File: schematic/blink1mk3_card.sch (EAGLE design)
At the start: 15 parts, among them U1 EFM32HG309F64G, X2 USBPCB2

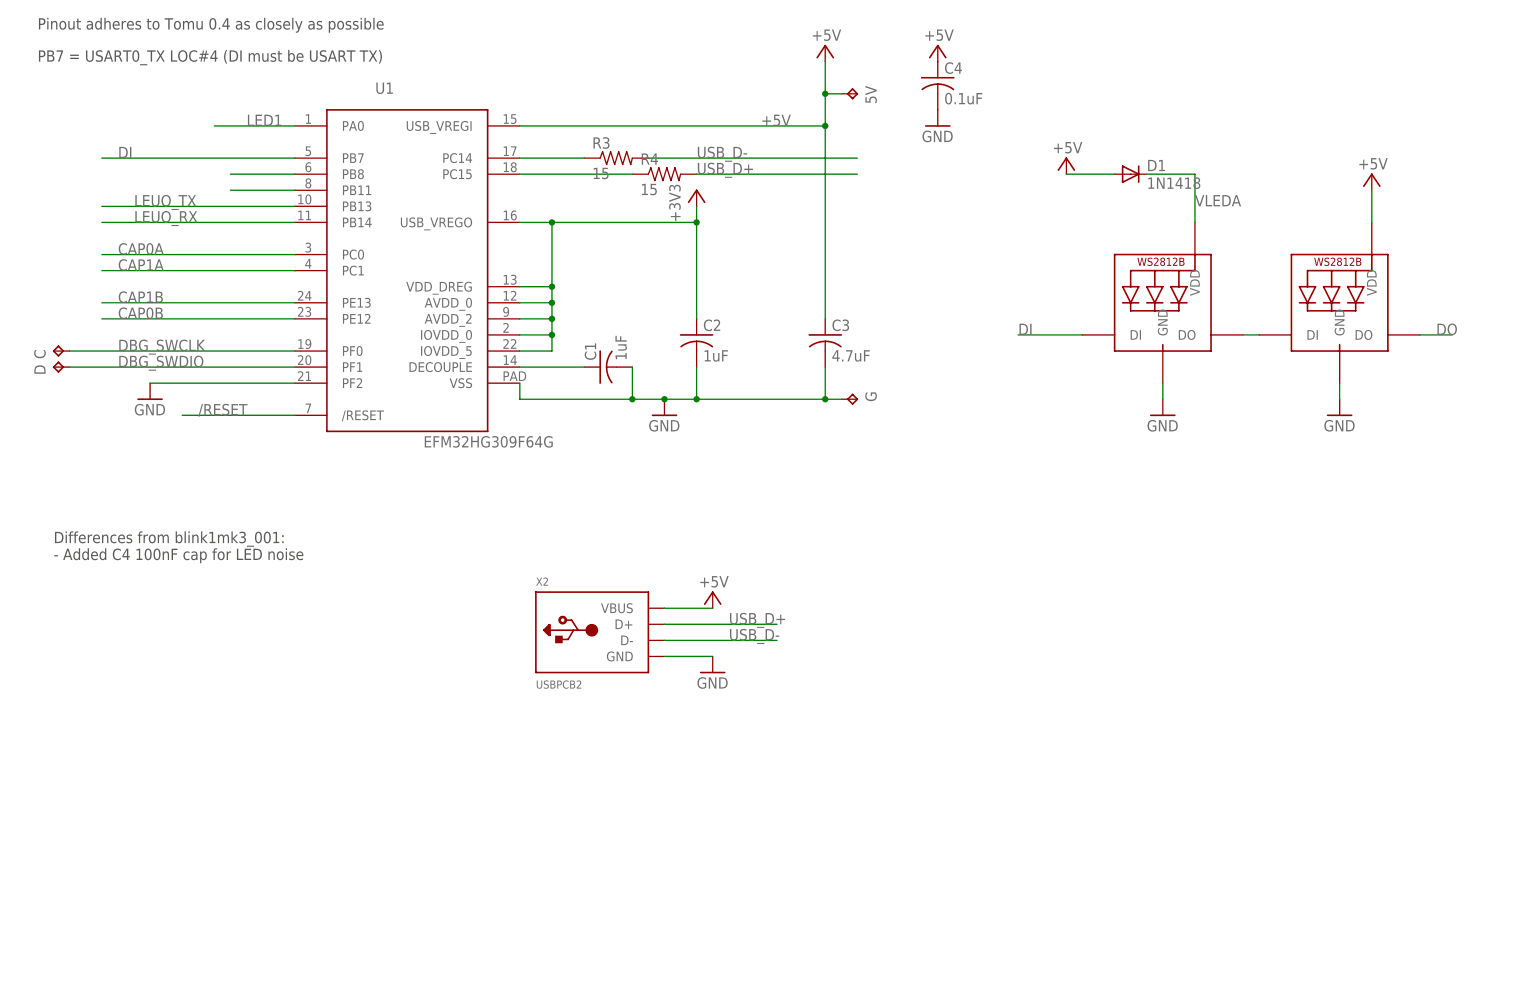
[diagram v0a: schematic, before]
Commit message: added business card variant, and 3535 LED variant
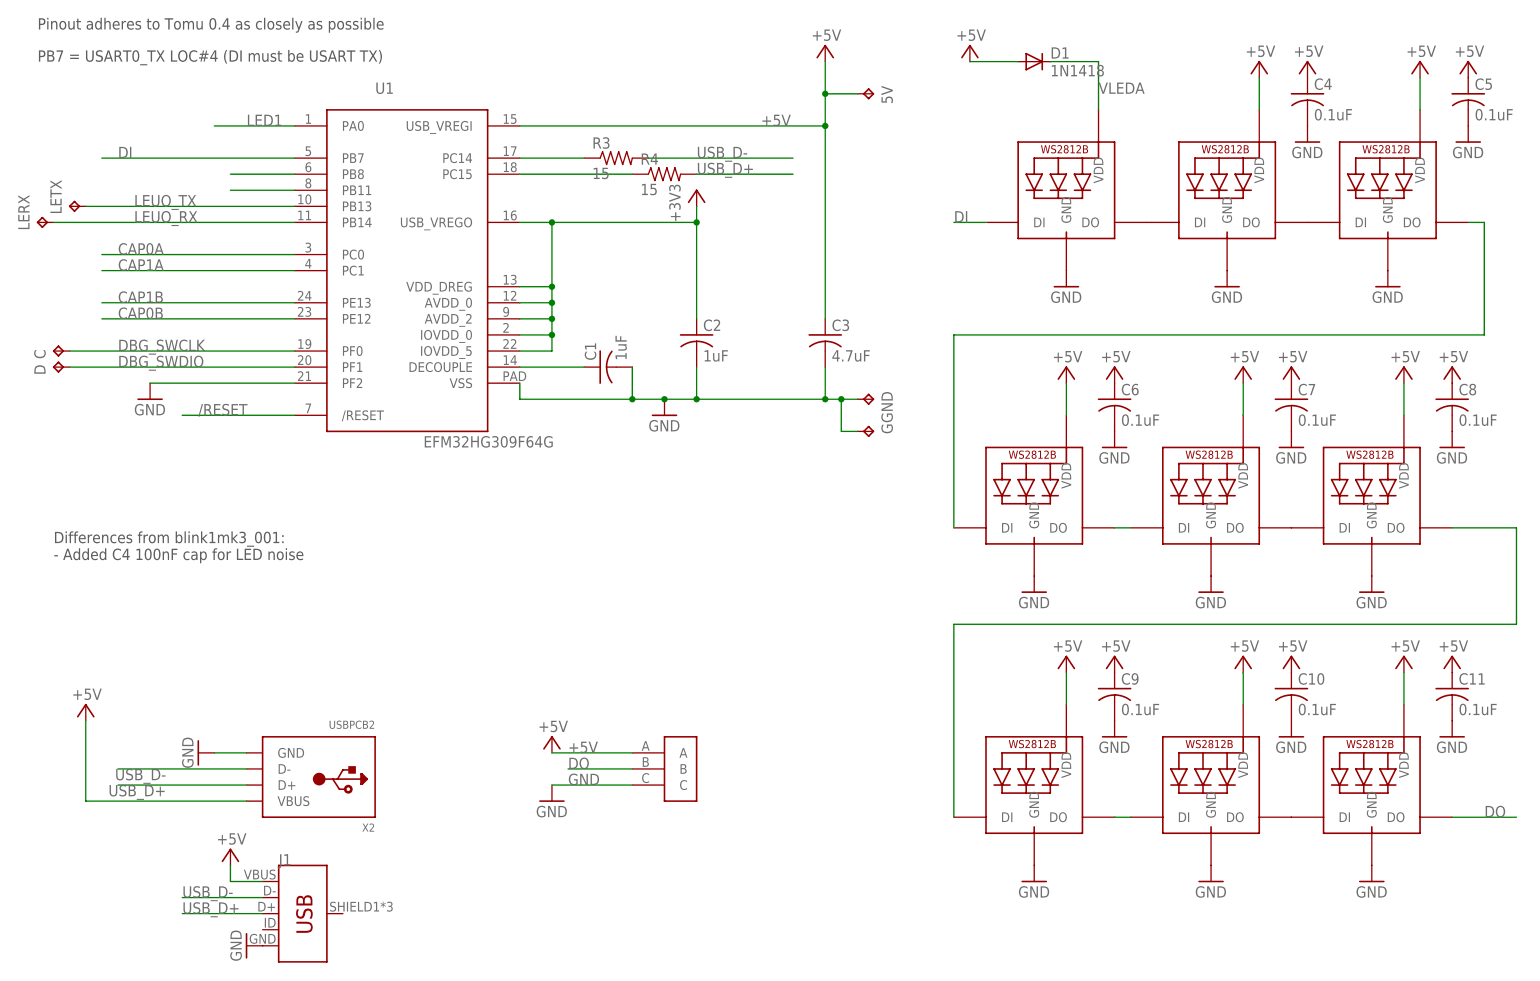
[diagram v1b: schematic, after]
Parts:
- added C10, C11, C5, C6, C7, C8, C9: 0.1uF, adafruit:C-USC0603
- added GND: TPTP14SQ, testpad:TPTP14SQ
- added J1: (no value), SparkFun-Connectors:USB_MICRO-B_FEMALE-SMT
- added LED3, LED4, LED5, LED6, LED7, LED8, LED9: WS2812B3535, adafruit:WS2812B3535
- added LERX, LETX: TPTP15R, testpad:TPTP15R
- added U$1: LED_STRIP_3P, NeoJoints:LED_STRIP_3P
- 5V, C, D: value TPTP10R -> TPTP15R; device testpad:TPTP10R -> testpad:TPTP15R
- C1, C2, C3, C4: device adafruit:C-USC0402 -> adafruit:C-USC0603
- G: value TPTP10R -> TPTP14SQ; device testpad:TPTP10R -> testpad:TPTP14SQ
- LED1, LED2: value WS2812B4020SIDE -> WS2812B3535; device todstuff:WS2812B4020SIDE -> adafruit:WS2812B3535
- R3, R4: device adafruit:R-US_R0402 -> adafruit:R-US_R0603
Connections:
- new net N$10: LED6.DO, LED7.DI
- new net N$4: LED7.DO, LED8.DI
- new net N$5: LED4.DO, LED5.DI
- new net N$6: LED5.DO, LED6.DI
- new net N$7: LED2.DO, LED3.DI
- new net N$8: LED3.DO, LED4.DI
- new net N$9: LED8.DO, LED9.DI
- net +5V: now also C10.1, C11.1, C5.1, C6.1, C7.1, C8.1, C9.1, J1.VBUS, LED3.VDD, LED4.VDD, LED5.VDD, LED6.VDD, LED7.VDD, LED8.VDD, LED9.VDD, U$1.A
- net DO: now also LED9.DO, U$1.B; no longer LED2.DO
- net GND: now also C10.2, C11.2, C5.2, C6.2, C7.2, C8.2, C9.2, GND.TP, J1.GND, LED3.GND, LED4.GND, LED5.GND, LED6.GND, LED7.GND, LED8.GND, LED9.GND, U$1.C
- net LEUO_RX: now also LERX.TP
- net LEUO_TX: now also LETX.TP
- net USB_D+: now also J1.D+
- net USB_D-: now also J1.D-
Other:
- moved on the sheet: 5V, C4, D1, G, X2
